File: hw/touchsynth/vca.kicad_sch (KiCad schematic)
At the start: 36 parts, among them J4 LINE OUT, Q12 MMBT3904, Q13 BC847BS, U11 TL072, U12 LM324

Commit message: Schematic v2: hand-drawn sheet layouts with wires; MIDI in DNP
- draw.py/gen_sch2.py/layouts.py: placement + wiring per block, automatic
  labels for remaining split nets, short detection, junctions, KiCad
  endpoint-only connection semantics
- all 7 sheets laid out (ladder drawn as a transistor stack, diff amps,
  integrator with reset, R-2R DAC, ...); ERC 0 violations, netlist == design,
  145 simulated elements match
- MIDI input parts marked DNP (footprints kept)
- docs/touchsynth_schematic.pdf

Co-Authored-By: Claude Opus 5.5 (1M context) <noreply@anthropic.com>
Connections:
- net CVV_A: no longer names the net of C41.1, R74.2, R75.1
- net CVV_B: no longer names the net of C42.1, R75.2, R76.1
- net LINEOUT: no longer names the net of C46.2, J4.1 (Pin_1), R92.1
- net VCAOUT: no longer names the net of C46.1, R89.2, R93.1, TP18.1, U11.7
- net VCA_DM: no longer names the net of R88.2, R89.1, U11.6 (-)
- net VCA_DP: no longer names the net of R90.2, R91.1, U11.5 (+)
- net VCA_IN1: no longer names the net of Q13.2 (B1), R81.2, R82.1, R85.1
- net VCA_IN2: no longer names the net of Q13.5 (B2), R83.1, R84.2
- net VCA_VI: no longer names the net of C44.2, R81.1
- net VIV_B: no longer names the net of Q12.1 (B), R78.2
- net VIV_E: no longer names the net of Q12.2 (E), R79.1, R80.2, U12.6 (-)
- net VIV_OUT: no longer names the net of R78.1, U12.7
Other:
- note added: "CV_VCA: PWM filter and V-to-I converter (470k pull-up guarantees zero current at CV = 0)"
- note added: "VCA: differential pair with offset trim, difference amplifier, line out, audio loopback"
- note removed: "Audio loopback to PD5"
- note removed: "CV_VCA filter and V-to-I converter"
- note removed: "Difference amplifier, line out"
- note removed: "Test points"
- note removed: "VCA core and offset trim"

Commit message: PCB placement by functional block, silkscreen art, discrete LED resistors
- gen_pcb.py / pcb_place.py: 100 x 100 mm 2-layer board; keys, LEDs, connectors and test points fixed,
  ICs anchored per block, remaining parts placed greedily by connectivity inside their block
- blocks tile the circuit area with a 0.35 mm street for the dashed silkscreen frames and a reserved
  title tab each (pcb_art.py); piano keybed with hatched black keys; logo, resonant saw and ladder
  response curves on the front; signal-flow diagram on the back
- LED resistor arrays replaced by 16 discrete 4.7k 0603 (basic part) next to each LED
- deterministic schematic UUIDs, net name labels for PCB parity, op-amp re-pairing, fab.py

Co-Authored-By: Claude Opus 5.5 (1M context) <noreply@anthropic.com>
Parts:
- removed R74, R78, R82, R83: 1k, Resistor_SMD:R_0603_1608Metric, symbol Device:R
- removed R75, R76, R79, R86, R87: 4.7k, Resistor_SMD:R_0603_1608Metric, symbol Device:R
- removed R77: 15k, Resistor_SMD:R_0603_1608Metric, symbol Device:R
- removed R80: 470k, Resistor_SMD:R_0603_1608Metric, symbol Device:R
- removed R81: 33k, Resistor_SMD:R_0603_1608Metric, symbol Device:R
- removed R84: 1M, Resistor_SMD:R_0603_1608Metric, symbol Device:R
- removed R85: 2M, Resistor_SMD:R_0603_1608Metric, symbol Device:R
- removed R88: 10k, Resistor_SMD:R_0603_1608Metric, symbol Device:R
- removed R89: 22k, Resistor_SMD:R_0603_1608Metric, symbol Device:R
- added R100: 1M, Resistor_SMD:R_0603_1608Metric, symbol Device:R
- added R101: 2M, Resistor_SMD:R_0603_1608Metric, symbol Device:R
- added R102, R103, R95: 4.7k, Resistor_SMD:R_0603_1608Metric, symbol Device:R
- added R104, R106, R109: 10k, Resistor_SMD:R_0603_1608Metric, symbol Device:R
- added R105, R107: 22k, Resistor_SMD:R_0603_1608Metric, symbol Device:R
- added R108: 100k, Resistor_SMD:R_0603_1608Metric, symbol Device:R
- added R110: 15k, Resistor_SMD:R_0603_1608Metric, symbol Device:R
- added R96: 470k, Resistor_SMD:R_0603_1608Metric, symbol Device:R
- added R97: 33k, Resistor_SMD:R_0603_1608Metric, symbol Device:R
- added R98, R99: 1k, Resistor_SMD:R_0603_1608Metric, symbol Device:R
- added unit 3 of U11
- R90: value 10k -> 1k; LCSC C25804 -> C21190; Sim RD3 -> R1V
- R91: value 22k -> 4.7k; LCSC C31850 -> C23162; Sim RD4 -> R2V
- R92: value 100k -> 4.7k; LCSC C25803 -> C23162; Note output bleeder -> (none); Sim (none) -> R3V
- R93: value 10k -> 15k; LCSC C25804 -> C22809; Sim RLB1 -> R4V
- R94: value 15k -> 1k; LCSC C22809 -> C21190; Sim RLB2 -> RBVV
- U11: Sim XDCO/XDIF -> XRDIF/XDIF
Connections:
- net +5V: now also R96.1
- net ADC_AUDIO: now also R109.2, R110.1; no longer R93.2, R94.1
- net GND: now also R93.2, R101.2, R108.2, R110.2, R95.2, U11.4 (V-); no longer R92.2, R94.2
- net PWM_VCA: now also R90.1
- net VCA_C1: now also R102.2, R104.1
- net VCA_C2: now also R103.2, R106.1; no longer R90.1
- net VP: now also R102.1, R103.1, U11.8 (V+)
- net VREF: now also R107.2, R98.2, R99.2; no longer R91.2
- net VTRIM: now also R100.1
- net XVCA: now also R92.2, R93.1
- net VCAOUT: now reaches C46.1, TP18.1, U11.7
- net VCAOUT: now also R105.2, R109.1; no longer R93.1
- net CVV_B: now reaches C42.1
- net CVV_B: now also R91.2, R92.1
- net VCA_VI: now reaches C44.2
- net VCA_VI: now also R97.1
- net CVV_A: now reaches R90.2, R91.1
- net CVV_A: now also C41.1; no longer U11.5 (+)
- net VIV_E: now reaches Q12.2 (E), U12.6 (-)
- net VIV_E: now also R95.1, R96.2
- net LINEOUT: now reaches C46.2, J4.1 (Pin_1)
- net LINEOUT: now also R108.1; no longer R92.1
- net VCA_IN1: now reaches Q13.2 (B1)
- net VCA_IN1: now also R101.1, R97.2, R98.1
- net VIV_B: now reaches Q12.1 (B)
- net VIV_B: now also R94.2
- net VCA_IN2: now reaches Q13.5 (B2)
- net VCA_IN2: now also R100.2, R99.1
- net VIV_OUT: now reaches U12.7
- net VIV_OUT: now also R94.1
- net VCA_DM: now reaches U11.6 (-)
- net VCA_DM: now also R104.2, R105.1
- new net VCA_DP: R106.2, R107.1, U11.5 (+)

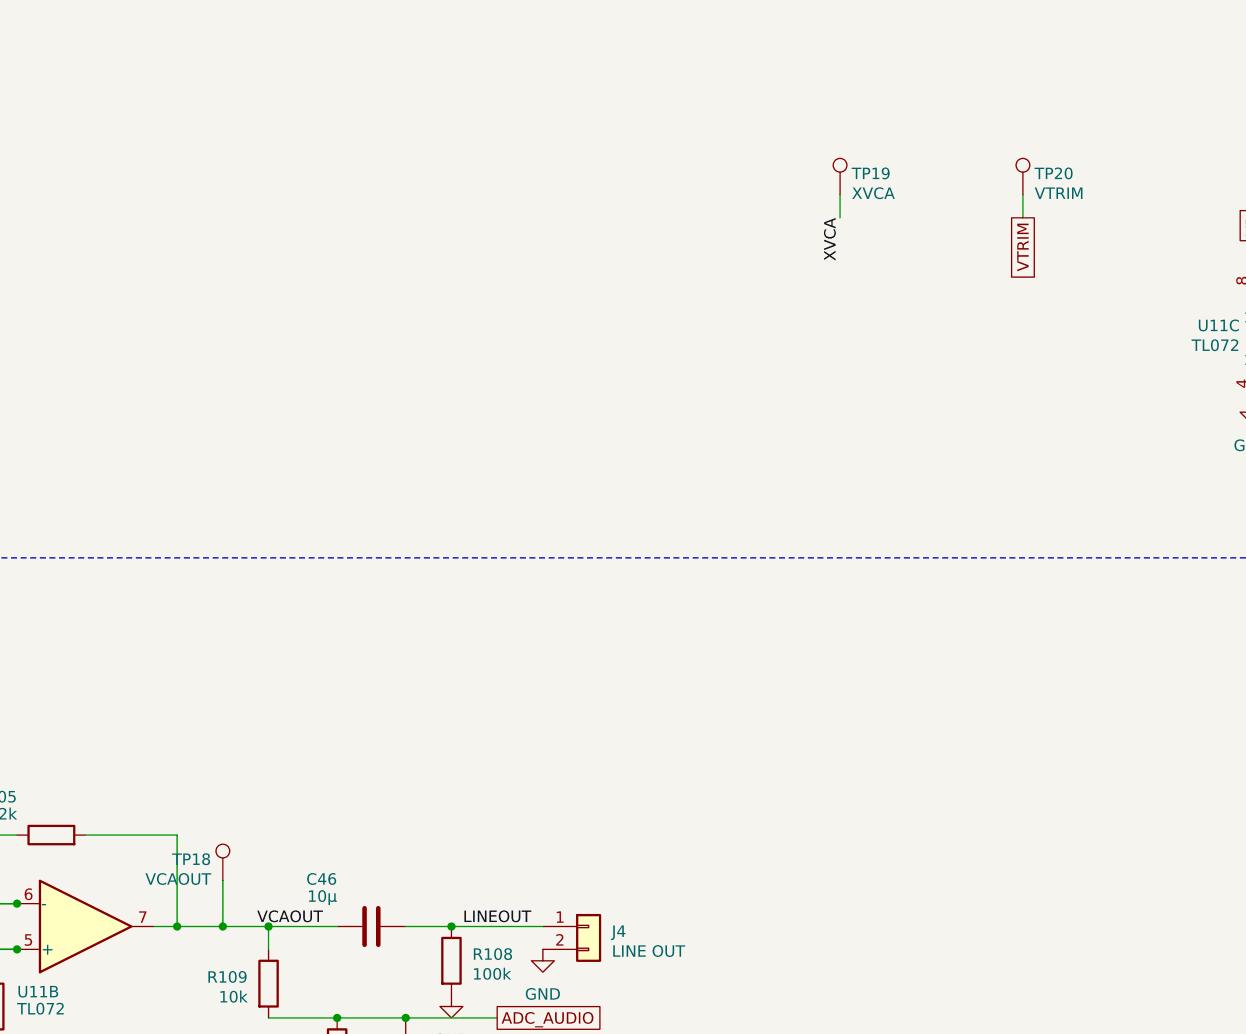
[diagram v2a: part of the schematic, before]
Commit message: 4-layer PCB: keys I/O row, trim DAC by the VCA, full routing and fab outputs
- 4 layers: F.Cu signals, In1 solid GND, In2 split power (VP analog / +5V digital / GND under the keys),
  B.Cu signals; no plane and no foreign tracks under the touch pads
- floorplan: analog blocks 72 x 36 mm in signal-flow order, right column MIDI / trim DAC / MCU,
  keys I/O row (touch muxes, LED shift registers) directly above the keys; shorter white keys,
  function pads flush with the keybed; test points inside their blocks, two THT scope-ground pins
- routing pipeline: plane stitch vias, pre-routed plane nets, Freerouting, GND via grid, island
  check, A* maze router for leftovers (pcb_maze.py), rip-up repair mode
- DRC: 0 violations, 0 unconnected, schematic parity OK; JLCPCB gerbers / BOM / CPL via fab.py
- silkscreen: back-side credits (design: cpldcpu & Claude Opus 5.5), vias kept out of the art

Co-Authored-By: Claude Opus 5.5 (1M context) <noreply@anthropic.com>
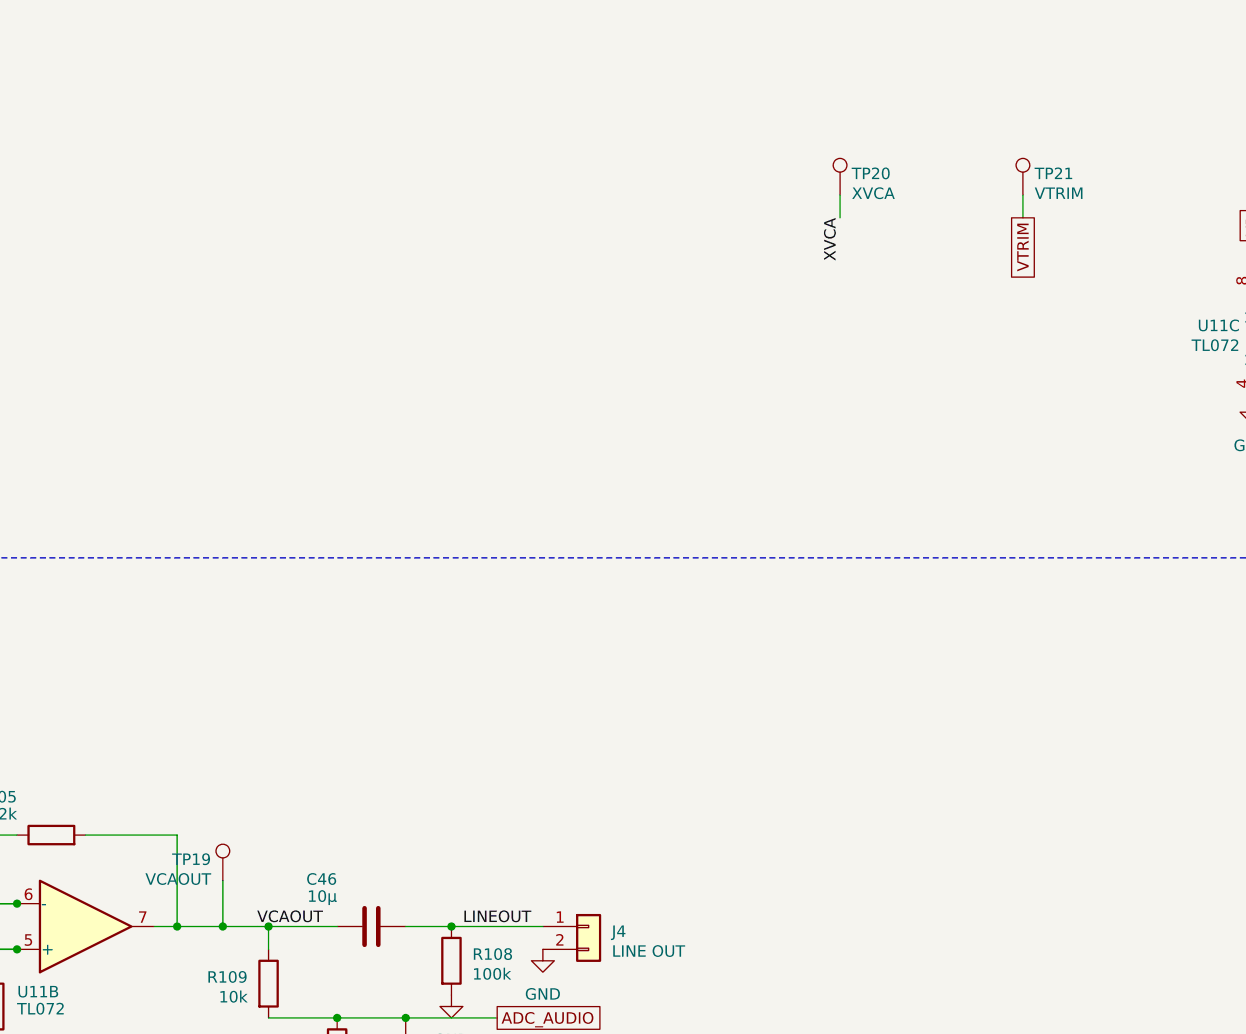
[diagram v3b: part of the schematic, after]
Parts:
- removed TP18: VCAOUT, TestPoint:TestPoint_Pad_D1.0mm, symbol Connector:TestPoint
- added TP21: VTRIM, TestPoint:TestPoint_Pad_D1.0mm, symbol Connector:TestPoint
- TP19: value XVCA -> VCAOUT
- TP20: value VTRIM -> XVCA
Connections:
- net VCAOUT: now also TP19.1
- net VTRIM: now also TP21.1; no longer TP20.1
- net XVCA: now also TP20.1; no longer TP19.1
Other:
- moved on the sheet: TP19, TP20
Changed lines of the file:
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@@
 		(on_board yes)
 		(dnp no)
-		(property "Reference" "TP18"
+		(property "Reference" "TP19"
 			(at 252.7 129.729 0)
 			(effects
@@
 			(project "touchsynth"
 				(path "/c42cd0d4-93b1-5178-97ee-fdd3025be2c6/dd8b73cc-ac1d-5e58-853a-b645944ed5f9"
-					(reference "TP18")
+					(reference "TP19")
 					(unit 1)
 				)
@@
 		(on_board yes)
 		(dnp no)
-		(property "Reference" "TP19"
+		(property "Reference" "TP20"
 			(at 323.88 53.529 0)
 			(effects
@@
 			(project "touchsynth"
 				(path "/c42cd0d4-93b1-5178-97ee-fdd3025be2c6/dd8b73cc-ac1d-5e58-853a-b645944ed5f9"
-					(reference "TP19")
+					(reference "TP20")
 					(unit 1)
 				)
@@
 		(on_board yes)
 		(dnp no)
-		(property "Reference" "TP20"
+		(property "Reference" "TP21"
 			(at 344.2 53.529 0)
 			(effects
@@
 			(project "touchsynth"
 				(path "/c42cd0d4-93b1-5178-97ee-fdd3025be2c6/dd8b73cc-ac1d-5e58-853a-b645944ed5f9"
-					(reference "TP20")
-					(unit 1)
-				)
+					(reference "TP21")
+					(unit 1)
+				)
